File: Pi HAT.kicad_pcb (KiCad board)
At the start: 2 copper layers, 65 x 41.5 mm, 90 parts, among them IC1 AD7730, J1 Screw_Terminal_01x04, J11 Conn_01x02_Male, J4 Barrel_Jack, J5 Screw_Terminal_01x03, J6 Screw_Terminal_01x03, J7 GPIO_CONNECTOR, J9 Conn_01x03_Male, K1 SANYOU_SRD_Form_C, K2 SANYOU_SRD_Form_C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

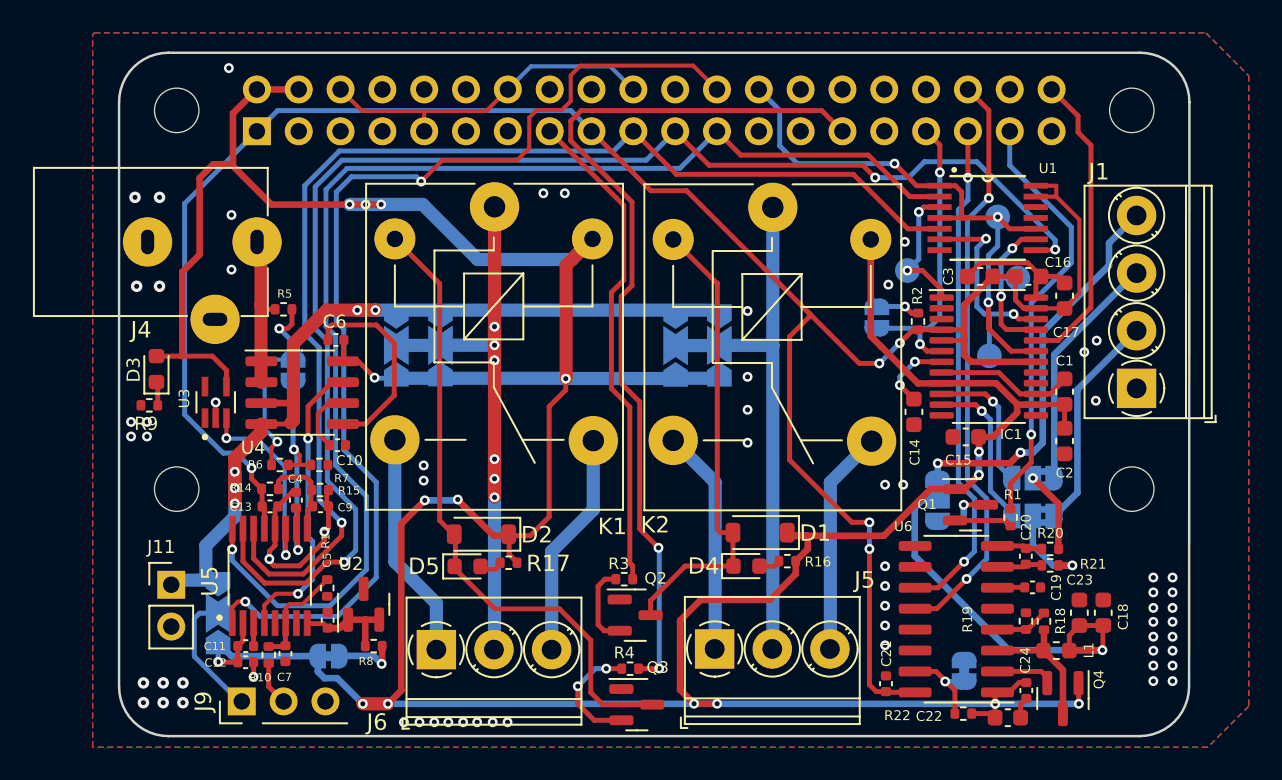
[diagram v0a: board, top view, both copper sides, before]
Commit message: Minor tweaks on the board, board pullback, and 8550 error spotted
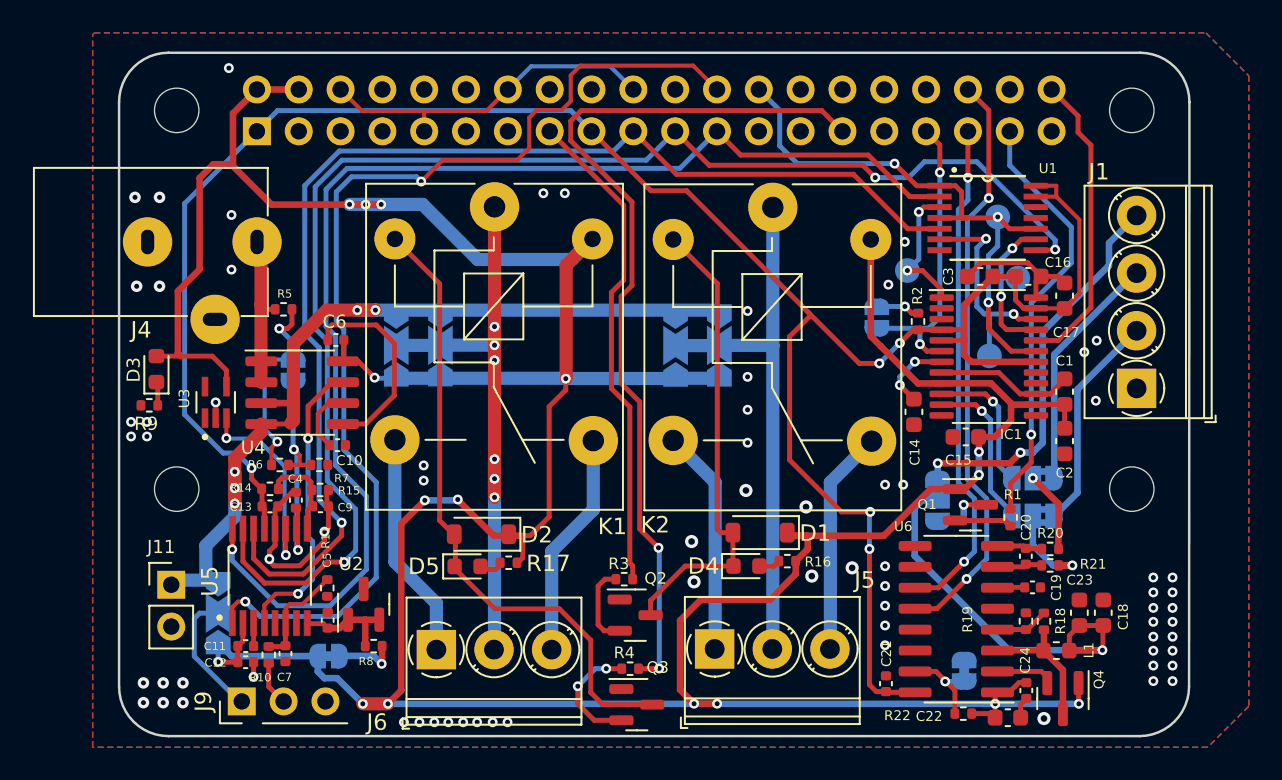
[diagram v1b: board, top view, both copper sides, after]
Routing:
- net /LOAD_CELL_EXC: track 24.2 -> 23.6 mm
- net GND: vias 65 -> 72

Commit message: Fixed BJT footprints and adc bridges
-1.1.x Fixed the BJT pinouts
-1.1.1 Fixed connections for adc jumpers
-1.1.2 Add keep-out zone near relay jumpers
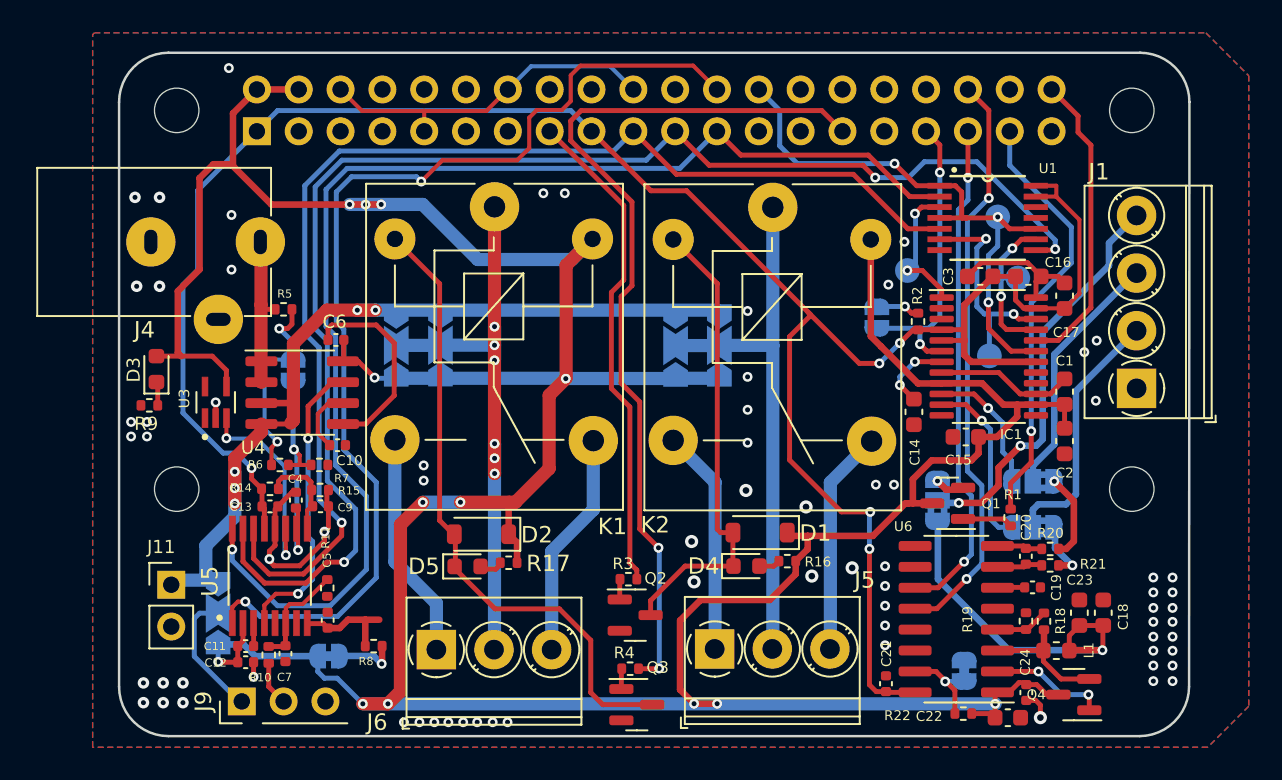
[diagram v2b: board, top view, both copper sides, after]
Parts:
- removed U2: CJ431, Package_TO_SOT_SMD:SOT-23
- U4: value ACS712xLCTR-20A -> ACS712x
- moved Q1 1.39 mm to (167.8, 118.4), turned to 180 degrees
- moved Q4 0.71 mm to (175.5, 130.0), turned to 180 degrees
- moved JP11 0.69 mm to (173.0, 119.9)
- moved R3 0.25 mm to (148.5, 123.0)
- moved J4 0.20 mm to (112.6, 102.6)
- moved JP9 0.19 mm to (173.0, 117.1)
- moved C24 0.12 mm to (172.6, 129.9)
- turned JP12 to 90 degrees
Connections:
- JP11 pad 1: /S- -> /INA-
- JP11 pad 2: /INA- -> /S-
- JP12 pad 1: /LOAD_CELL_EXC -> /EXC+
- JP12 pad 2: /EXC+ -> /LOAD_CELL_EXC
- JP9 pad 1: /S+ -> /INA+
- JP9 pad 2: /INA+ -> /S+
- L1 pad 2: Net-(Q4-C) -> Net-(Q4-E)
- Q1 pad 1: +5V -> Net-(Q1-B)
- Q1 pad 2: Net-(Q1-B) -> /LOAD_CELL_PWR
- Q1 pad 3: /LOAD_CELL_PWR -> +5V
- Q2 pad 1: GND -> Net-(Q2-E)
- Q2 pad 2: Net-(Q2-B) -> GND
- Q3 pad 1: GND -> Net-(Q3-E)
- Q3 pad 2: Net-(Q3-B) -> GND
- Q4 pad 1: +5V -> Net-(Q4-B)
- Q4 pad 2: Net-(Q4-B) -> Net-(Q4-E)
- Q4 pad 3: Net-(Q4-C) -> +5V
- R18 pad 1: Net-(Q4-C) -> Net-(Q4-E)
- R3 pad 1: Net-(Q2-B) -> Net-(Q2-E)
- R4 pad 1: Net-(Q3-B) -> Net-(Q3-E)
- U6 pad 3: Net-(Q4-C) -> Net-(Q4-E)
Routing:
- net Net-(Q4-C): track 8.42 -> 0.00 mm
- net Net-(Q4-E): track 0.00 -> 7.95 mm
- net Net-(Q3-B): track 7.24 -> 0.00 mm, vias 2 -> 0
- net +5V: track 246.0 -> 240.2 mm, vias 16 -> 13
- net Net-(Q2-B): track 5.07 -> 0.00 mm
- net Net-(Q4-B): track 3.52 -> 7.08 mm, vias 0 -> 2
- net /EXC+: track 25.0 -> 22.0 mm
- net /S-: track 13.3 -> 15.5 mm
- net /LOAD_CELL_PWR: track 3.43 -> 1.90 mm
- net /INA-: track 5.52 -> 4.06 mm
- net Net-(Q3-E): track 0.00 -> 1.25 mm
- net Net-(Q2-E): track 0.00 -> 1.24 mm
- net /LOAD_CELL_EXC: track 23.6 -> 24.6 mm
- net +BATT: track 8.58 -> 9.52 mm
- net /AIN1-: track 9.72 -> 10.5 mm
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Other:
- board text added: "RPi0 Instrument. HAT v1.1.2 Montšo Mokake 19/01/2024"
- board text removed: "RPi0 Instrument. HAT v1.0.0 Montšo Mokake 09/12/2023"

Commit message: Added gnd stitching vias. Fixed 5v track
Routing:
- net +5V: track 240.2 -> 240.5 mm, vias 13 -> 14
- net GND: vias 72 -> 110

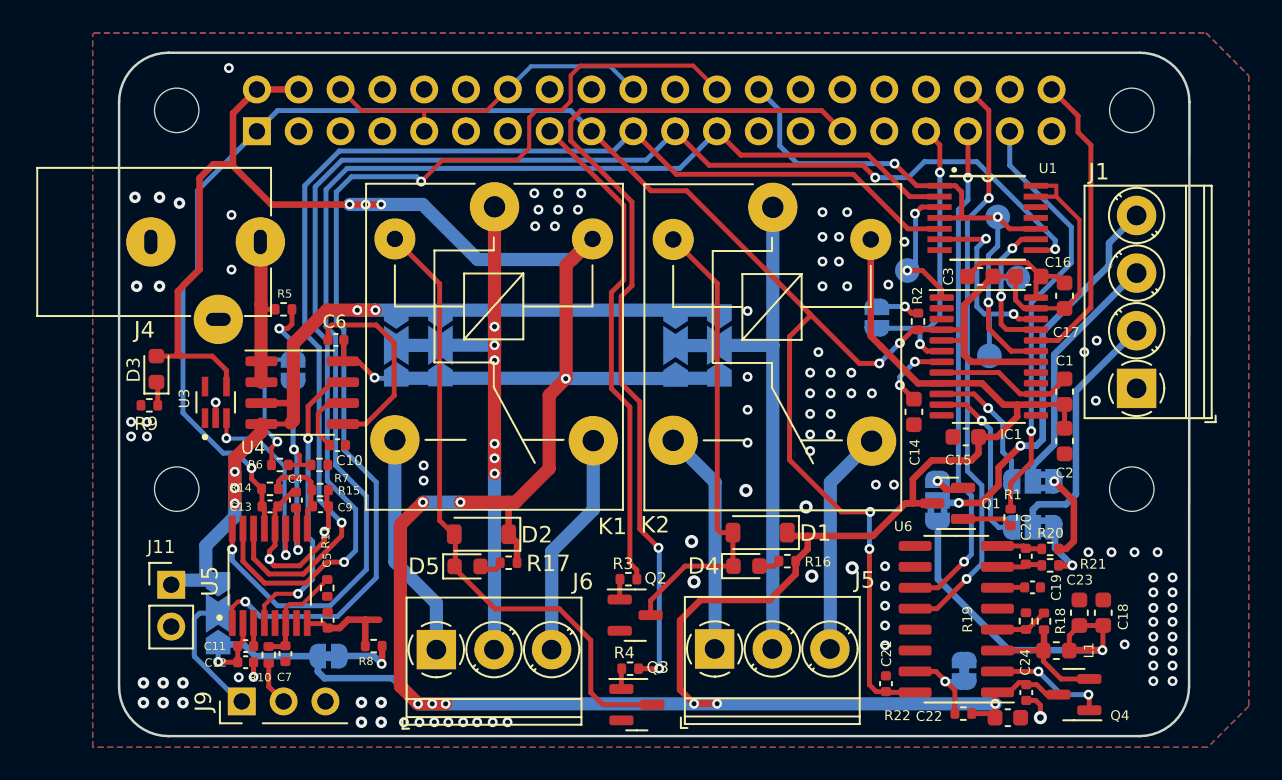
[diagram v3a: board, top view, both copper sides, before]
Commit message: Connected NO2 to COM1. Annonated relays.
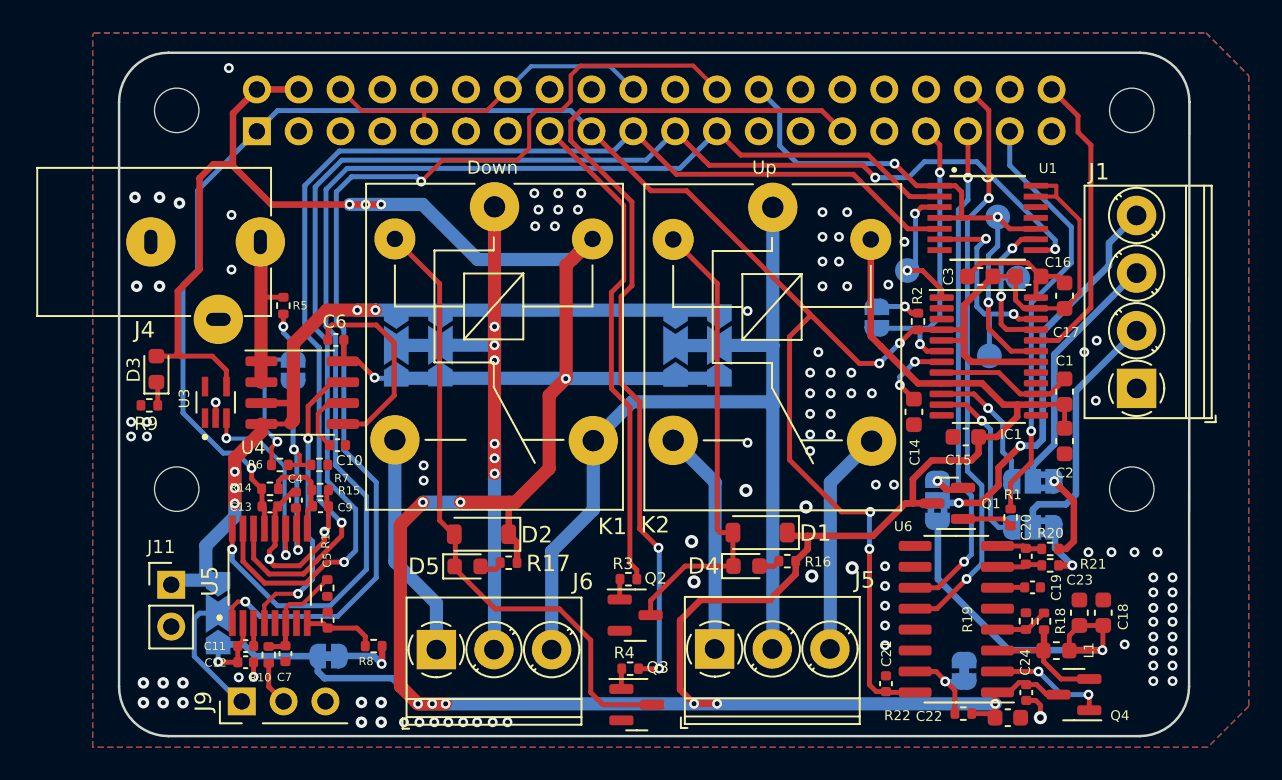
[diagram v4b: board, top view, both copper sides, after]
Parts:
- moved R5 0.22 mm to (127.5, 106.4), turned to -90 degrees
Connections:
- J4 pad 3: (no net) -> unconnected-(J4-Pad3)
- J6 pad 3: /Relays/NC2 -> /Relays/COM1
- K1 pad 4: /Relays/NC2 -> /Relays/COM1
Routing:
- net /Relays/COM1: track 32.7 -> 58.4 mm
- net /Relays/NC2: track 13.7 -> 0.00 mm
- net /Power Monitor/ADC4: track 6.30 -> 4.44 mm
- net Net-(JP6-A): track 12.4 -> 11.4 mm
- net GND: vias 110 -> 108
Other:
- board text added: "+VE"
- board text added: "-VE"
- board text added: "Down"
- board text added: "RPi0 Instrument. HAT v1.2.0 Montšo Mokake 07/06/2024"
- board text added: "S+"
- board text added: "S-"
- board text added: "Up"
- board text removed: "RPi0 Instrument. HAT v1.1.2 Montšo Mokake 19/01/2024"

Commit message: Ammended it to have the jumper connection
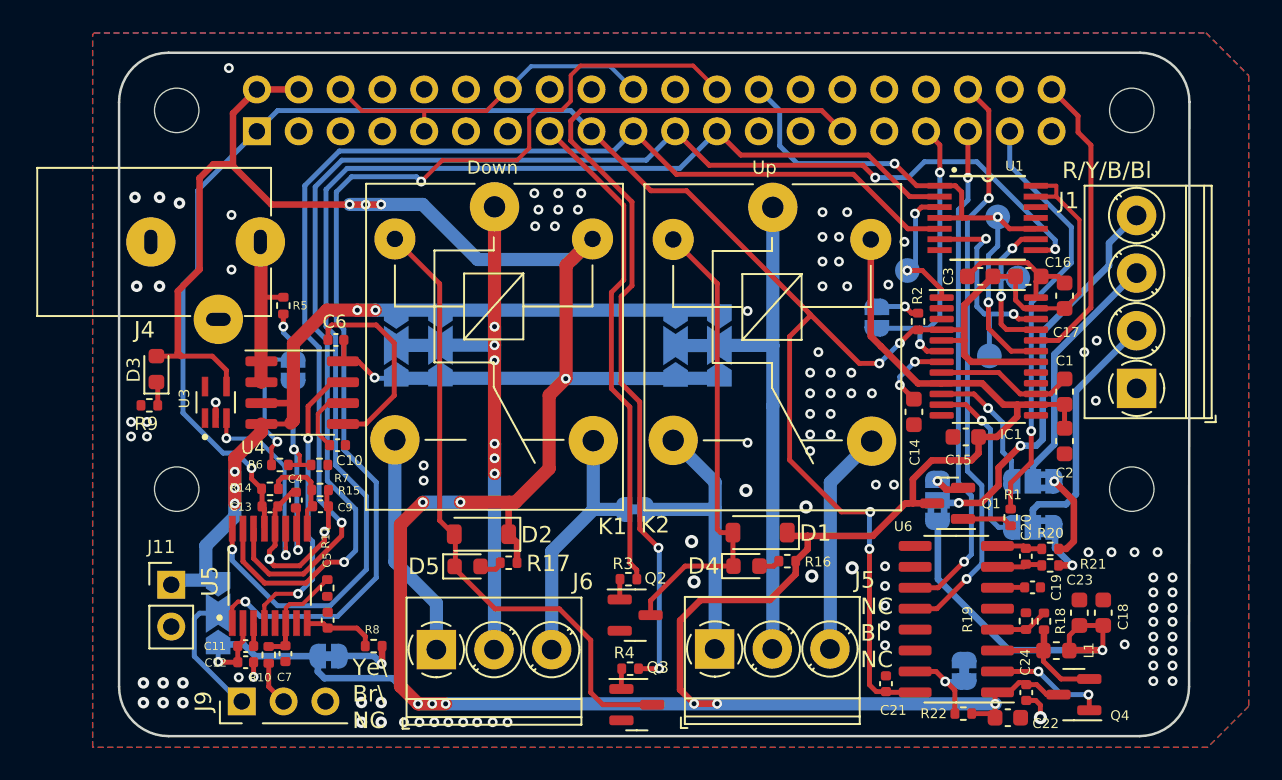
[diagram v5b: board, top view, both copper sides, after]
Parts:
- added JP13: Jumper_2_Small_Bridged, Jumper:SolderJumper-2_P1.3mm_Bridged_RoundedPad1.0x1.5mm, B.Cu at (148.8, 118.8)
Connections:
- J6 pad 3: /Relays/COM1 -> /Relays/NC2
- K1 pad 4: /Relays/COM1 -> /Relays/NC2
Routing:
- net /Relays/COM1: track 58.4 -> 32.7 mm
- net /Relays/NC2: track 0.00 -> 15.6 mm
- net /Relays/NO1: track 13.8 -> 18.0 mm
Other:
- board text added: "NC Bl NC"
- board text added: "R/Y/B/Bl"
- board text added: "Ye\ Br\ NC"

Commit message: Modified the PCB to have a greater spacing on anything Relay 2ndary side related
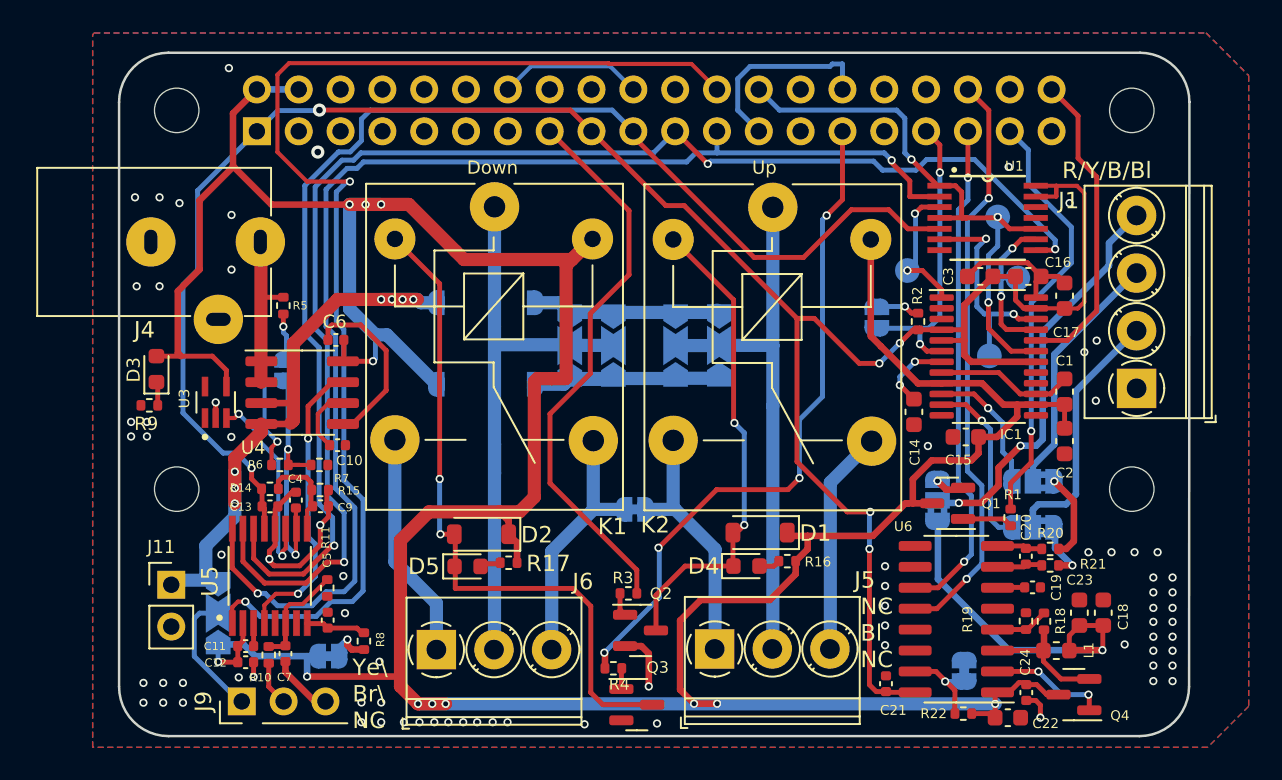
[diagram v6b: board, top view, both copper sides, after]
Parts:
- added JP14: Jumper_2_Small_Bridged, UCT:Jumper_Open_wide, B.Cu at (139.8, 111.2)
- added JP15: Jumper_2_Small_Bridged, UCT:Jumper_Open_wide, B.Cu at (139.8, 106.2)
- D4, D5: value Blue_LED -> Red_LED
- R16, R17: value 120R -> 1k
- moved JP4 10.5 mm to (144.9, 108.8)
- moved JP2 10.5 mm to (147.6, 108.8)
- moved R4 1.02 mm to (147.6, 128.4), turned to 180 degrees
- moved Q2 0.98 mm to (149.2, 126.2)
- moved R3 0.86 mm to (148.5, 123.9)
- moved R8 0.67 mm to (132.4, 126.8), turned to 90 degrees
- moved JP6 0.40 mm to (127.7, 110.3)
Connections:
- JP1 pad 1: /Power Monitor/Batt_Sensed -> Net-(JP1-A)
- JP1 pad 3: +5V -> Net-(JP1-B)
- JP2 pad 1: /Power Monitor/Batt_Sensed -> Net-(JP1-A)
- JP2 pad 3: +5V -> Net-(JP1-B)
- JP3 pad 1: /Power Monitor/Batt_Sensed -> Net-(JP1-A)
- JP3 pad 3: +5V -> Net-(JP1-B)
- JP4 pad 1: /Power Monitor/Batt_Sensed -> Net-(JP1-A)
- JP4 pad 3: +5V -> Net-(JP1-B)
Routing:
- net /Power Monitor/Batt_Sensed: track 52.1 -> 36.2 mm, vias 5 -> 7
- net Net-(JP1-B): track 0.00 -> 14.1 mm
- net /GPIO5: track 54.6 -> 41.2 mm, vias 2 -> 4
- net Net-(JP1-A): track 0.00 -> 11.6 mm
- net /GPIO8_SPI_CE0_N: track 64.8 -> 73.6 mm
- net GND: track 67.3 -> 72.9 mm, vias 108 -> 77
- net +5V: track 240.5 -> 235.5 mm, vias 14 -> 12
- net /GPIO22_GEN3: track 30.0 -> 34.2 mm
- net /GPIO10_SPI_MOSI: track 73.1 -> 77.2 mm
- net /Relays/NO1: track 18.0 -> 15.5 mm
- net Net-(D2-A): track 38.8 -> 41.1 mm, vias 0 -> 2
- net +3.3V: track 136.7 -> 138.2 mm, vias 5 -> 6
- net /Power Monitor/ADC6: track 15.3 -> 16.5 mm
- net Net-(JP5-B): track 3.87 -> 2.68 mm
- net Net-(D1-A): track 28.5 -> 29.6 mm, vias 0 -> 2
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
